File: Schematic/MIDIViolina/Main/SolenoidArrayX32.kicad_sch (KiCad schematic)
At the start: 128 parts, among them J10 Solenoid, J11 Solenoid, J12 Solenoid, J13 Solenoid, J14 Solenoid, J15 Solenoid, J16 Solenoid, J17 Solenoid, J18 Solenoid, J19 Solenoid, J20 Solenoid, J21 Solenoid, J22 Solenoid, J23 Solenoid, J24 Solenoid, J25 Solenoid, J26 Solenoid, J27 Solenoid, J28 Solenoid, J29 Solenoid, J30 Solenoid, J31 Solenoid, J32 Solenoid, J33 Solenoid, J34 Solenoid, J35 Solenoid, J36 Solenoid, J37 Solenoid, J38 Solenoid, J39 Solenoid, J40 Solenoid, J41 Solenoid, Q10 IRF540N, Q11 IRF540N, Q12 IRF540N, Q13 IRF540N, Q14 IRF540N, Q15 IRF540N, Q16 IRF540N, Q17 IRF540N, Q18 IRF540N, Q19 IRF540N, Q20 IRF540N, Q21 IRF540N, Q22 IRF540N, Q23 IRF540N, Q24 IRF540N, Q25 IRF540N, Q26 IRF540N, Q27 IRF540N, Q28 IRF540N, Q29 IRF540N, Q30 IRF540N, Q31 IRF540N, Q32 IRF540N, Q33 IRF540N, Q34 IRF540N, Q35 IRF540N, Q36 IRF540N, Q5 IRF540N, Q6 IRF540N, Q7 IRF540N, Q8 IRF540N, Q9 IRF540N

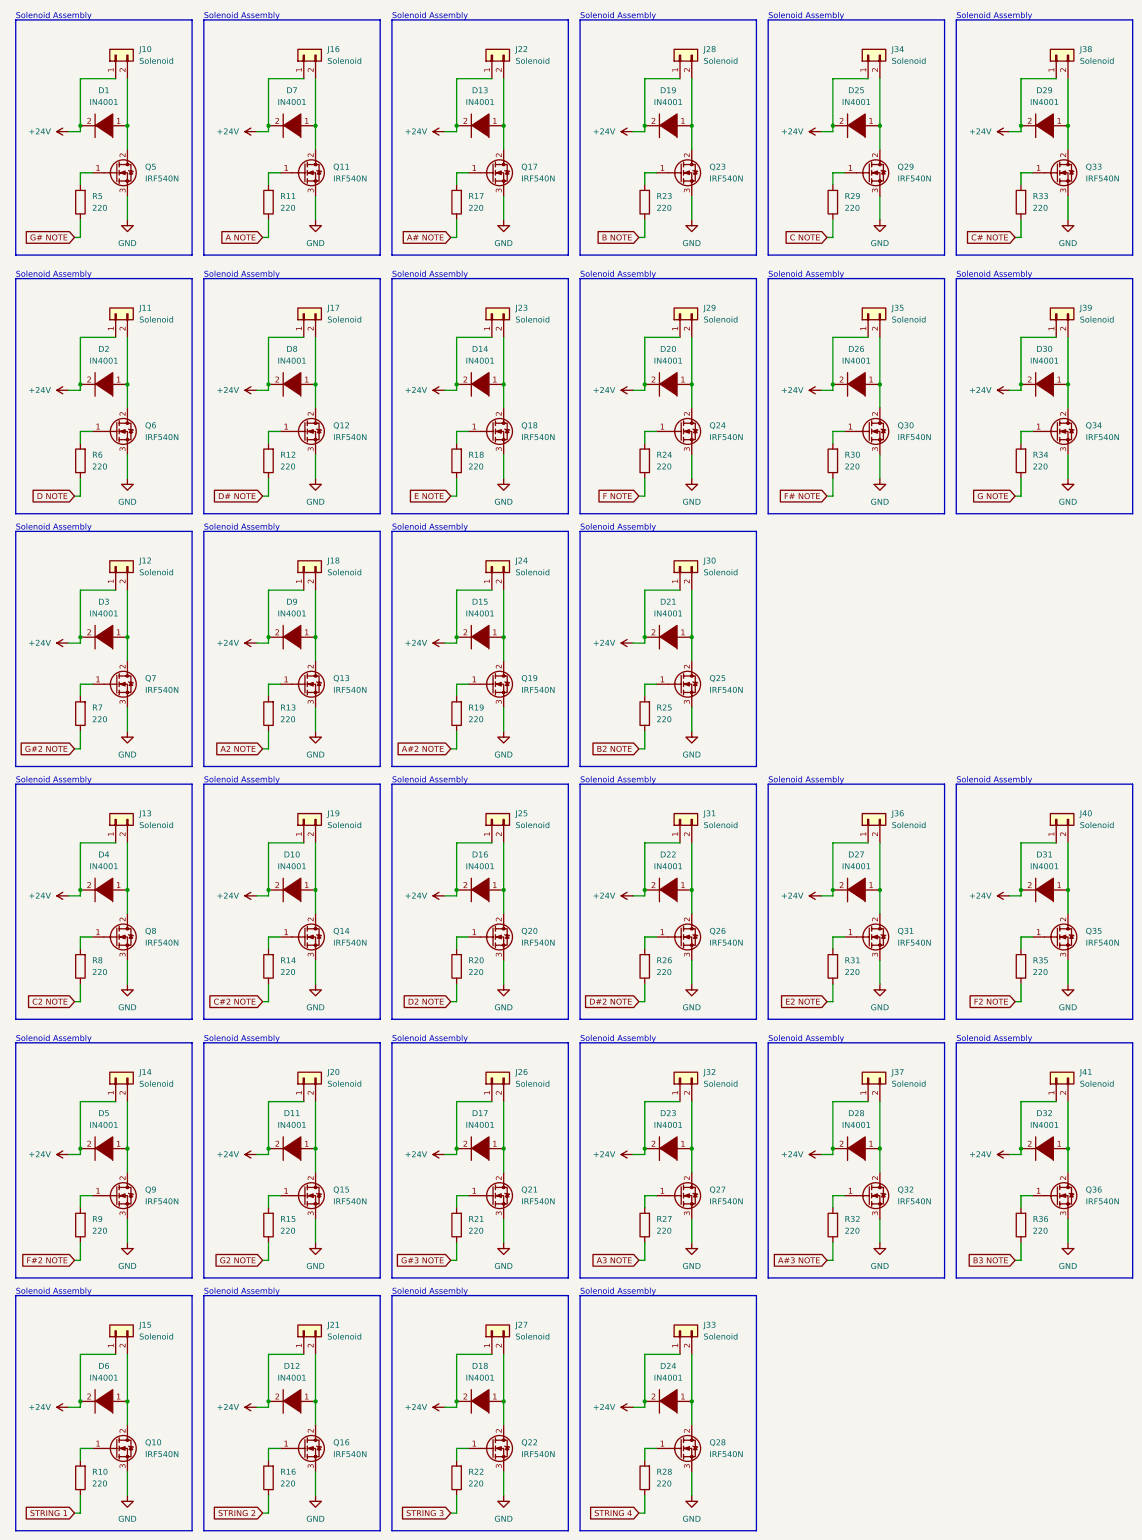
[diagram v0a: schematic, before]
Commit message: CNC Toolpaths and PCB updates
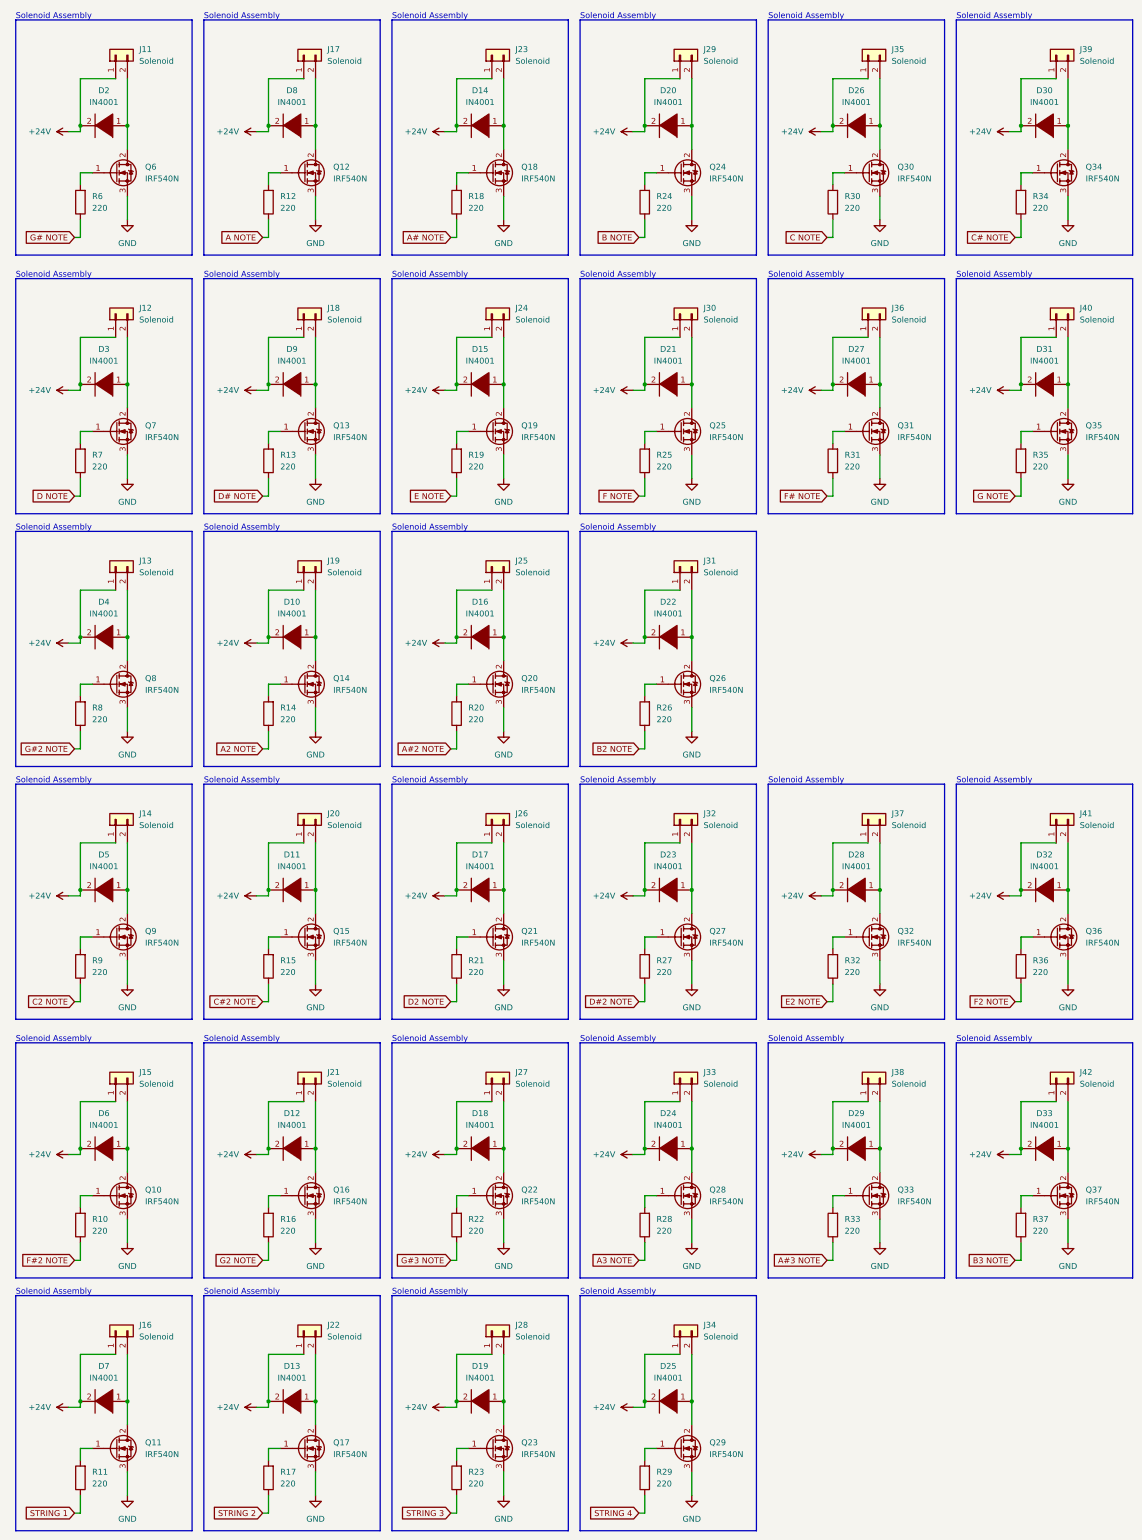
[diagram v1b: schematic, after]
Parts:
- renumbered D9 to D10, D10 to D11, D11 to D12, D12 to D13, D13 to D14, D14 to D15, D15 to D16, D16 to D17, D17 to D18, D18 to D19, D1 to D2, D19 to D20, D20 to D21, D21 to D22, D22 to D23, D23 to D24, D24 to D25, D25 to D26, D26 to D27, D27 to D28, D28 to D29, D2 to D3, D29 to D30, D30 to D31, D31 to D32, D32 to D33, D3 to D4, D4 to D5, D5 to D6, D6 to D7, D7 to D8, D8 to D9, J10 to J11, J11 to J12, J12 to J13, J13 to J14, J14 to J15, J15 to J16, J16 to J17, J17 to J18, J18 to J19, J19 to J20, J20 to J21, J21 to J22, J22 to J23, J23 to J24, J24 to J25, J25 to J26, J26 to J27, J27 to J28, J28 to J29, J29 to J30, J30 to J31, J31 to J32, J32 to J33, J33 to J34, J34 to J35, J35 to J36, J36 to J37, J37 to J38, J38 to J39, J39 to J40, J40 to J41, J41 to J42, Q9 to Q10, Q10 to Q11, Q11 to Q12, Q12 to Q13, Q13 to Q14, Q14 to Q15, Q15 to Q16, Q16 to Q17, Q17 to Q18, Q18 to Q19, Q19 to Q20, Q20 to Q21, Q21 to Q22, Q22 to Q23, Q23 to Q24, Q24 to Q25, Q25 to Q26, Q26 to Q27, Q27 to Q28, Q28 to Q29, Q29 to Q30, Q30 to Q31, Q31 to Q32, Q32 to Q33, Q33 to Q34, Q34 to Q35, Q35 to Q36, Q36 to Q37, Q5 to Q6, Q6 to Q7, Q7 to Q8, Q8 to Q9, R9 to R10, R10 to R11, R11 to R12, R12 to R13, R13 to R14, R14 to R15, R15 to R16, R16 to R17, R17 to R18, R18 to R19, R19 to R20, R20 to R21, R21 to R22, R22 to R23, R23 to R24, R24 to R25, R25 to R26, R26 to R27, R27 to R28, R28 to R29, R29 to R30, R30 to R31, R31 to R32, R32 to R33, R33 to R34, R34 to R35, R35 to R36, R36 to R37, R5 to R6, R6 to R7, R7 to R8, R8 to R9
